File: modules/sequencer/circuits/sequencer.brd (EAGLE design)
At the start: 100 x 80 mm, 35 parts, among them IC2 LM324N

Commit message: sequencer design
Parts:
- added 1K, 1K1, 1K2, R23: 1k, adafruit:0207/12
- added 2N4400: (no value), transistor-neu-to92:TO92-EBC
- added DAISY_CHAIN, INPUTS: (no value), pinhead:1X06
- added MPS2907: (no value), transistor:TO92-CBE
- added R20: 10k, adafruit:0207/12
- added R21: 100k, adafruit:0207/12
- added RESET_BUTTON: (no value), pinhead:1X02
- added SPLIT_SELECT: (no value), pinhead:2X03
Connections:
- removed net VSS: CD4163.8
- new net COUNTER_POWER: CD4017.16, MPS2907.C
- new net HALF_STEP: 1K1.2, CD4163.11, R23.2
- new net N$2: CD4163.7, R20.2
- new net N$30: 1K.1, 2N4400.C, SPLIT_SELECT.3
- new net N$31: 2N4400.B, R23.1
- new net N$32: POWER.1, RESET_BUTTON.1
- new net N$36: 1K1.1, SPLIT_SELECT.5
- new net N$37: MPS2907.B, SPLIT_SELECT.2, SPLIT_SELECT.4, SPLIT_SELECT.6
- new net N$38: 1K2.1, SPLIT_SELECT.1
- net -12V: now also DAISY_CHAIN.4, INPUTS.4
- net 12V: now also DAISY_CHAIN.3, INPUTS.3
- net 3.3V: now also 2N4400.E, CD4017.15, CD4163.8, DAISY_CHAIN.6, INPUTS.6
- net 5V: now also 1K.2, 1K2.2, CD4163.16, DAISY_CHAIN.5, INPUTS.5, MPS2907.E, R20.1, R21.1, RESET_BUTTON.2; no longer CD4017.16, POWER.1
- net CLK_IN: now also CD4163.2, DAISY_CHAIN.1, INPUTS.1
- net N$10: now also R19.2; no longer R1.2
- net N$3: now also R1.2; no longer R19.2
- net N$4: now also R13.2; no longer R18.2
- net N$5: now also R14.2; no longer R17.2
- net N$6: now also R15.2; no longer R16.2
- net N$7: now also R16.2; no longer R15.2
- net N$8: now also R17.2; no longer R14.2
- net N$9: now also R18.2; no longer R13.2
- net RESET: now also CD4163.1, CD4163.9, R21.2; no longer CD4017.15
- net START_STOP: now also DAISY_CHAIN.2, INPUTS.2
- net VDD: no longer CD4163.16

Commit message: Sync
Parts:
- removed C3: 2.2uf, adafruit:E2,5-6E
- removed C4: 1uf, adafruit:E2,5-6E
- removed INPUTS: (no value), pinhead:1X06
- removed LM7905: (no value), linear:TO220H
- removed POWER: (no value), pinhead:1X04
- added 1: 4017N, 40xx:DIL16
- added D10, D11, D12, D13, D14, D15, D16, D9: 1N4004, adafruit:DO41-10
- added INPUTS1: (no value), pinhead:1X06
- added R40, R56: 10k, SparkFun-Resistors:AXIAL-0.3
- added R41, R42, R43, R44, R45, R46, R47, R48, R49, R50, R51, R52, R53, R54, R55: 1k, SparkFun-Resistors:AXIAL-0.3
- added WIDTH_SELECTION1: (no value), pinhead:2X07
- moved CD4163 66.1 mm to (83.8, 14.0)
- moved DAISY_CHAIN 6.35 mm to (-74.9, -213.4)
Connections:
- removed net -5V: C4.-, IC2.11, LM7905.3
- removed net START_STOP: CD4017.13, DAISY_CHAIN.2, INPUTS.2
- removed net VDD: C3.-, LM7905.2
- new net DIV_CLK: CD4017.14, D10.C, D11.C, D12.C, D9.C, DAISY_CHAIN.1, R40.P$1
- new net GATE_OUT: R47.P$2, R48.P$2, R56.P$1
- new net GND: 1.13, 1.8
- new net GNDA: R40.P$2, R56.P$2, WIDTH_SELECTION1.10, WIDTH_SELECTION1.12, WIDTH_SELECTION1.14, WIDTH_SELECTION1.2, WIDTH_SELECTION1.4, WIDTH_SELECTION1.6, WIDTH_SELECTION1.8
- new net N$56: 1.15, 1.9
- new net N$57: 1.3, D16.A, D9.A
- new net N$58: 1.2, D10.A, D13.A
- new net N$59: 1.4, D11.A, D14.A
- new net N$60: 1.7, D12.A, D15.A
- new net N$61: 1.6, R48.P$1
- new net N$62: R41.P$2, R47.P$1, R49.P$2, WIDTH_SELECTION1.13
- new net N$63: R41.P$1, R42.P$2, R50.P$2, WIDTH_SELECTION1.11
- new net N$64: 1.10, R51.P$1
- new net N$65: R43.P$1, R44.P$2, R52.P$2, WIDTH_SELECTION1.7
- new net N$66: R44.P$1, R45.P$2, R53.P$2, WIDTH_SELECTION1.5
- new net N$67: R45.P$1, R46.P$2, R54.P$2, WIDTH_SELECTION1.3
- new net N$68: R46.P$1, R55.P$2, WIDTH_SELECTION1.1
- new net N$69: 1.5, R49.P$1
- new net N$70: 1.1, R50.P$1
- new net N$71: R42.P$1, R43.P$2, R51.P$2, WIDTH_SELECTION1.9
- new net N$72: D15.C, R52.P$1
- new net N$73: D14.C, R53.P$1
- new net N$74: D13.C, R54.P$1
- new net N$75: D16.C, R55.P$1
- net -12V: now also IC2.11, INPUTS1.3; no longer INPUTS.4, POWER.3
- net 12V: now also IC2.4, INPUTS1.2; no longer INPUTS.3, POWER.2
- net 3.3V: now also INPUTS1.4; no longer C3.+, C4.+, INPUTS.6, LM7905.1, POWER.4
- net 5V: now also 1.16; no longer IC2.4, INPUTS.5
- net CLK_IN: now also 1.14, INPUTS1.5; no longer CD4017.14, DAISY_CHAIN.1, INPUTS.1
- net N$32: now also INPUTS1.1; no longer POWER.1

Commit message: divider
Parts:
- removed 1: 4017N, 40xx:DIL16
- removed D10, D11, D12, D13, D14, D15, D16, D9: 1N4004, adafruit:DO41-10
- removed R40, R56: 10k, SparkFun-Resistors:AXIAL-0.3
- removed R41, R42, R43, R44, R45, R46, R47, R48, R49, R50, R51, R52, R53, R54, R55: 1k, SparkFun-Resistors:AXIAL-0.3
- removed WIDTH_SELECTION1: (no value), pinhead:2X07
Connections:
- removed net DIV_CLK: CD4017.14, D10.C, D11.C, D12.C, D9.C, DAISY_CHAIN.1, R40.P$1
- removed net GATE_OUT: R47.P$2, R48.P$2, R56.P$1
- removed net GND: 1.13, 1.8
- removed net GNDA: R40.P$2, R56.P$2, WIDTH_SELECTION1.10, WIDTH_SELECTION1.12, WIDTH_SELECTION1.14, WIDTH_SELECTION1.2, WIDTH_SELECTION1.4, WIDTH_SELECTION1.6, WIDTH_SELECTION1.8
- removed net N$56: 1.15, 1.9
- removed net N$57: 1.3, D16.A, D9.A
- removed net N$58: 1.2, D10.A, D13.A
- removed net N$59: 1.4, D11.A, D14.A
- removed net N$60: 1.7, D12.A, D15.A
- removed net N$61: 1.6, R48.P$1
- removed net N$62: R41.P$2, R47.P$1, R49.P$2, WIDTH_SELECTION1.13
- removed net N$63: R41.P$1, R42.P$2, R50.P$2, WIDTH_SELECTION1.11
- removed net N$64: 1.10, R51.P$1
- removed net N$65: R43.P$1, R44.P$2, R52.P$2, WIDTH_SELECTION1.7
- removed net N$66: R44.P$1, R45.P$2, R53.P$2, WIDTH_SELECTION1.5
- removed net N$67: R45.P$1, R46.P$2, R54.P$2, WIDTH_SELECTION1.3
- removed net N$68: R46.P$1, R55.P$2, WIDTH_SELECTION1.1
- removed net N$69: 1.5, R49.P$1
- removed net N$70: 1.1, R50.P$1
- removed net N$71: R42.P$1, R43.P$2, R51.P$2, WIDTH_SELECTION1.9
- removed net N$72: D15.C, R52.P$1
- removed net N$73: D14.C, R53.P$1
- removed net N$74: D13.C, R54.P$1
- removed net N$75: D16.C, R55.P$1
- net 5V: no longer 1.16
- net CLK_IN: now also CD4017.14, DAISY_CHAIN.1; no longer 1.14

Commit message: Sequencer design complete
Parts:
- removed MPS2907: (no value), transistor:TO92-CBE
- added 1K3, 1K4: 1k, adafruit:0207/12
- added 2N1, 2N2: (no value), transistor-neu-to92:TO92-EBC
- added C2: 220uf, rcl:E2,5-6E
- added C3: 100nf, rcl:C025-024X044
- added D1: 1N4004, adafruit:DO41-10
- added GATE_POT, OUT, RESET_AFTER_2, RESET_AFTER_4: (no value), pinhead:1X02
- added R22, R24, R25: 10k, adafruit:0207/12
- moved INPUTS1 319.1 mm to (38.1, 7.62)
- moved RESET_BUTTON 267.8 mm to (50.8, 7.62)
- moved SPLIT_SELECT 259.7 mm to (43.2, 29.2)
- moved 1K2 255.6 mm to (40.6, 19.1), turned to 270 degrees
- moved 2N4400 245.5 mm to (62.2, 26.7), turned to 90 degrees
- moved 1K1 245.4 mm to (45.7, 19.1), turned to 270 degrees
- moved R21 244.3 mm to (72.4, 39.4), turned to 270 degrees
- moved R23 242.0 mm to (48.3, 19.1), turned to 270 degrees
- moved DAISY_CHAIN 241.1 mm to (21.6, 7.62)
- moved 1K 235.2 mm to (43.2, 19.1), turned to 270 degrees
- moved LED2 210.3 mm to (55.9, 66.0)
- moved LED3 210.3 mm to (55.9, 58.4)
- moved LED5 210.3 mm to (55.9, 43.2)
- moved LED6 210.3 mm to (55.9, 35.6)
- moved LED7 210.3 mm to (55.9, 27.9)
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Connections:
- removed net 3.3V: 2N4400.E, CD4017.15, CD4017.8, CD4163.8, DAISY_CHAIN.6, IC2.3, IC2.5, INPUTS1.4, LED1.K, LED2.K, LED3.K, LED4.K, LED5.K, LED6.K, LED7.K, LED8.K, POTS.17
- new net GATE: OUT.2, R24.1
- new net GND: 2N1.E, 2N2.E, 2N4400.E, CD4017.13, CD4017.8, CD4163.8, DAISY_CHAIN.6, IC2.3, IC2.5, INPUTS1.4, LED1.K, LED2.K, LED3.K, LED4.K, LED5.K, LED6.K, LED7.K, LED8.K, POTS.17, R20.1, R22.2
- new net N$35: 2N2.B, D1.C, R24.2
- new net N$39: 2N2.C, C2.+, R25.1
- new net N$40: 1K3.1, 2N1.C
- new net N$41: 1K4.1, GATE_POT.2
- new net N$42: 2N1.B, C2.-, GATE_POT.1
- net 5V: now also 1K3.2, 1K4.2, R25.2; no longer MPS2907.E, R20.1
- net CLK_IN: now also C3.1
- net COUNTER_POWER: now also IC2.8, IC2.9; no longer MPS2907.C
- net CV_OUT: now also OUT.1
- net N$1: now also CD4017.15, CD4017.9, R22.1, RESET_AFTER_2.1, RESET_AFTER_4.1; no longer CD4017.12, CD4163.3
- net N$2: now also C3.2, D1.A; no longer CD4163.7
- net N$37: now also IC2.10; no longer MPS2907.B
- net N$5: now also RESET_AFTER_2.2
- net N$8: now also RESET_AFTER_4.2
- net RESET: now also CD4163.7
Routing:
- net GND: track 0.00 -> 253.9 mm
- net CLK_IN: track 0.00 -> 200.7 mm
- net 5V: track 0.00 -> 109.7 mm
- net COUNTER_POWER: track 0.00 -> 72.1 mm
- net N$10: track 0.00 -> 71.6 mm
- net HALF_STEP: track 0.00 -> 69.2 mm
- net N$5: track 0.00 -> 67.0 mm
- net N$35: track 0.00 -> 66.9 mm
- net CV_OUT: track 0.00 -> 56.9 mm
- net N$7: track 0.00 -> 53.7 mm, vias 0 -> 1
- net N$4: track 0.00 -> 50.1 mm
- net N$3: track 0.00 -> 49.1 mm
- net RESET: track 0.00 -> 48.8 mm
- net N$9: track 0.00 -> 46.6 mm
- net N$6: track 0.00 -> 44.8 mm
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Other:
- board size 100 x 80 mm -> 68.2 x 80 mm

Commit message: Seq board
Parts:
- removed 1K, 1K2: 1k, adafruit:0207/12
- removed 2N1, 2N4400: (no value), transistor-neu-to92:TO92-EBC
- removed C3: 100nf, rcl:C025-024X044
- removed CD4163: 4163N, 40xx:DIL16
- removed DAISY_CHAIN: (no value), pinhead:1X06
- removed R24, R25: 10k, adafruit:0207/12
- removed SPLIT_SELECT: (no value), pinhead:2X03
- added C1: 0.01uf, rcl:C025-024X044
- added C4: 0.1uf, rcl:C025-024X044
- added IC1: LM555N, adafruit:DIL08-ROUND
- added LED9: (no value), adafruit:LED5MM
- 1K1: value 1k -> 100k
- 1K4: value 1k -> 10k
- D1: device adafruit:DO41-10 -> diode:DO41-10
- R21: value 100k -> 100
- R23: value 1k -> 330
- moved R21 191.6 mm to (15.2, -143.5), turned to 0 degrees
- moved 1K1 182.9 mm to (15.2, -161.3), turned to 0 degrees
- moved D1 179.1 mm to (14.0, -174.0)
- moved R23 178.3 mm to (15.2, -156.2), turned to 0 degrees
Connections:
- removed net COUNTER_POWER: CD4017.16, IC2.8, IC2.9
- removed net HALF_STEP: 1K1.2, CD4163.11, R23.2
- removed net N$37: IC2.10, SPLIT_SELECT.2, SPLIT_SELECT.4, SPLIT_SELECT.6
- removed net N$38: 1K2.1, SPLIT_SELECT.1
- removed net N$39: 2N2.C, C2.+, R25.1
- removed net N$40: 1K3.1, 2N1.C
- removed net N$41: 1K4.1, GATE_POT.2
- removed net N$42: 2N1.B, C2.-, GATE_POT.1
- removed net RESET: CD4163.1, CD4163.10, CD4163.7, CD4163.9, R21.2
- new net N$33: C4.1, D1.A, IC1.2, R20.1
- new net N$34: C1.1, IC1.5
- net -12V: no longer DAISY_CHAIN.4
- net 12V: no longer DAISY_CHAIN.3
- net 5V: now also C2.+, CD4017.16, D1.C, IC1.4, IC1.8, INPUTS1.1, R20.2, RESET_BUTTON.1; no longer 1K.2, 1K2.2, 1K3.2, CD4163.16, DAISY_CHAIN.5, R21.1, R25.2, RESET_BUTTON.2
- net CLK_IN: now also 2N2.B; no longer C3.1, CD4163.2, DAISY_CHAIN.1
- net GATE: now also 1K1.2; no longer R24.1
- net GND: now also C1.2, GATE_POT.1, IC1.1, R23.1; no longer 2N1.E, 2N4400.E, CD4163.8, DAISY_CHAIN.6, R20.1
- net N$1: now also RESET_BUTTON.2
- net N$10: no longer R19.2
- net N$2: now also 1K3.1, C4.2; no longer C3.2, D1.A, R20.2
- net N$3: no longer R1.2
- net N$30: now also LED9.K, R23.2; no longer 1K.1, 2N4400.C, SPLIT_SELECT.3
- net N$31: now also GATE_POT.2, R21.1; no longer 2N4400.B, R23.1
- net N$32: now also 1K3.2, 1K4.1, 2N2.C; no longer INPUTS1.1, RESET_BUTTON.1
- net N$35: now also C2.-, IC1.6, IC1.7, R21.2; no longer 2N2.B, D1.C, R24.2
- net N$36: now also IC1.3, LED9.A; no longer SPLIT_SELECT.5
- net N$4: no longer R13.2
- net N$5: no longer R14.2
- net N$6: no longer R15.2
- net N$7: no longer R16.2
- net N$8: no longer R17.2
- net N$9: no longer R18.2
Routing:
- net COUNTER_POWER: track 72.1 -> 0.00 mm
- net HALF_STEP: track 69.2 -> 0.00 mm
- net N$35: track 66.9 -> 0.00 mm
- net RESET: track 48.8 -> 0.00 mm
- net N$42: track 44.8 -> 0.00 mm
- net 5V: track 109.7 -> 66.7 mm
- net N$37: track 36.1 -> 0.00 mm
- net N$40: track 34.6 -> 0.00 mm
- net GND: track 253.9 -> 225.5 mm
- net N$39: track 27.5 -> 0.00 mm
- net N$41: track 25.9 -> 0.00 mm
- net N$30: track 23.4 -> 0.00 mm
- net N$32: track 19.8 -> 0.00 mm
- net CLK_IN: track 200.7 -> 183.1 mm
- net N$6: track 44.8 -> 28.2 mm
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
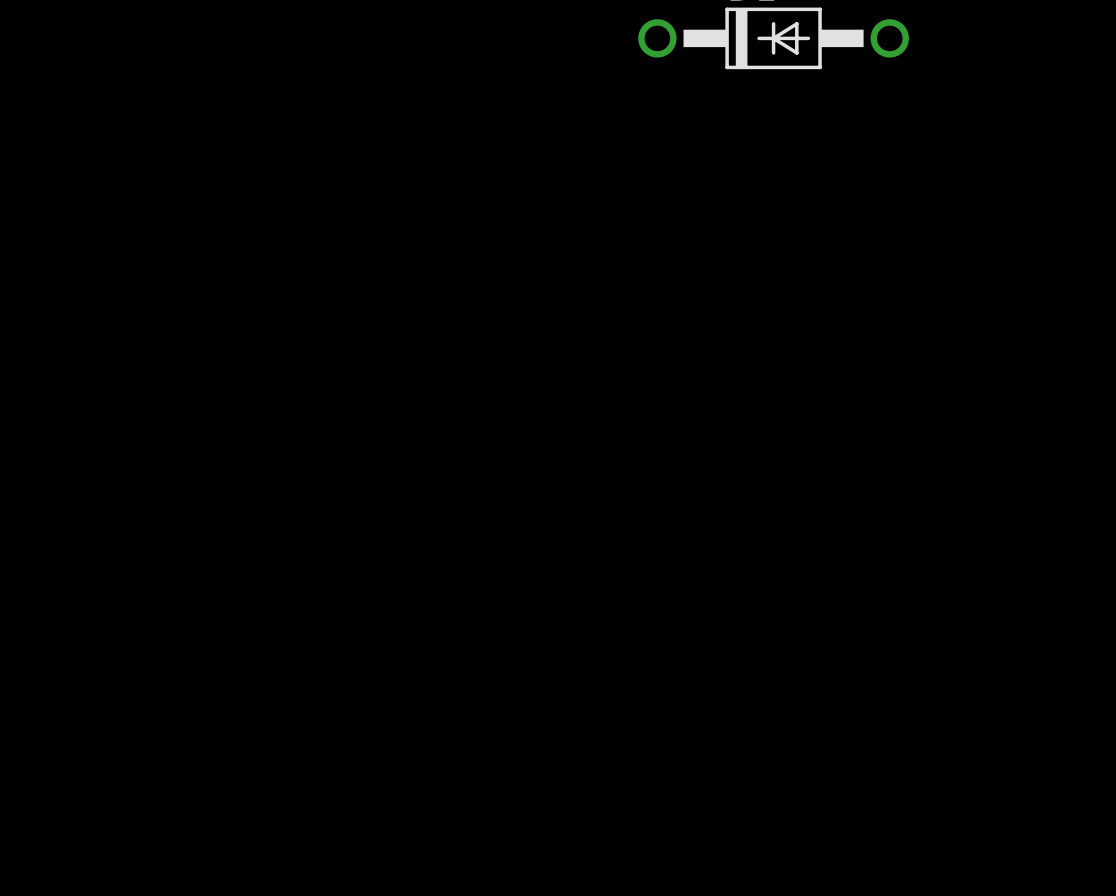
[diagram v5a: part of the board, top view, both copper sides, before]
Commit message: Adding counter to seq
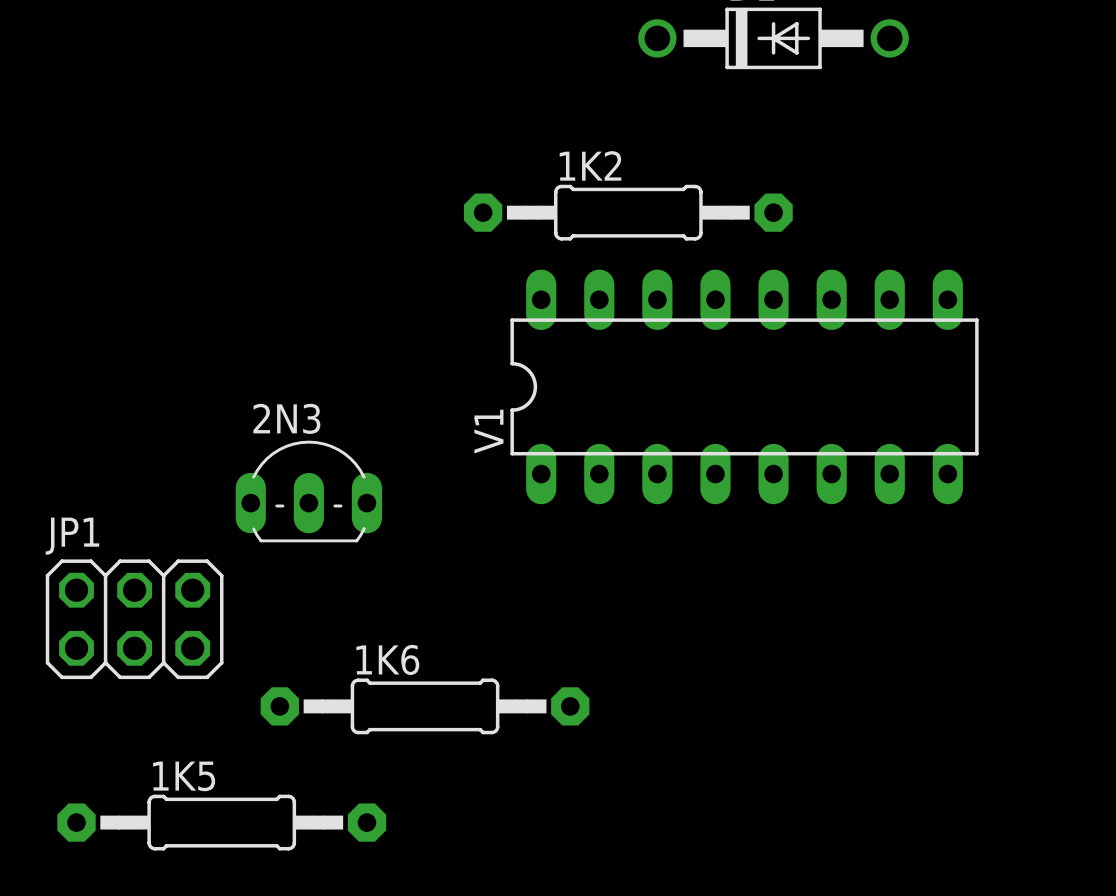
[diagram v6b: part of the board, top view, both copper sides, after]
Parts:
- added 1K2, 1K6: 1k, adafruit:0207/12
- added 1K5: 10k, adafruit:0207/12
- added 2N3: (no value), transistor-neu-to92:TO92-EBC
- added JP1: (no value), pinhead:2X03
- added V1: 74161N, 74ttl-din:DIL16
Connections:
- new net +UB: V1.16
- new net -UB: V1.8
- new net COUNTER_POWER: IC2.8, IC2.9
- new net N$37: 1K5.2, 2N3.B
- new net N$38: 1K5.1, JP1.4, V1.11
- new net N$39: 1K2.2, 1K6.2, 2N3.C
- new net N$40: 1K2.1, JP1.6
- new net N$42: IC2.10, JP1.1, JP1.3, JP1.5
- new net Q1: V1.14
- new net Q2: V1.13
- new net Q3: V1.12
- net 5V: now also 1K6.1, JP1.2
- net CLK_IN: now also V1.2
- net GND: now also 2N3.E
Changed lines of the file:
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@@
 <?xml version="1.0" encoding="utf-8"?>
 <!DOCTYPE eagle SYSTEM "eagle.dtd">
-<eagle version="9.6.2">
+<eagle version="9.5.2">
 <drawing>
 <settings>
@@
 <attribute name="VALUE" x="11.938" y="-176.784" size="1.27" layer="27" ratio="10"/>
 </element>
+<element name="1K2" library="adafruit" library_urn="urn:adsk.eagle:library:420" package="0207/12" package3d_urn="urn:adsk.eagle:package:6240598/1" value="1k" x="7.62" y="-181.61" smashed="yes">
+<attribute name="NAME" x="4.445" y="-180.213" size="1.27" layer="25" ratio="10"/>
+<attribute name="VALUE" x="5.334" y="-182.2958" size="1.27" layer="27" ratio="10"/>
+</element>
+<element name="V1" library="74ttl-din" library_urn="urn:adsk.eagle:library:84" package="DIL16" package3d_urn="urn:adsk.eagle:package:922/2" value="74161N" x="12.7" y="-189.23" smashed="yes">
+<attribute name="NAME" x="2.159" y="-192.151" size="1.27" layer="25" ratio="10" rot="R90"/>
+<attribute name="POPULARITY" value="0" x="12.7" y="-189.23" size="1.778" layer="27" display="off"/>
+<attribute name="VALUE" x="5.207" y="-189.865" size="1.27" layer="27" ratio="10"/>
+</element>
+<element name="2N3" library="transistor-neu-to92" library_urn="urn:adsk.eagle:library:397" package="TO92-EBC" package3d_urn="urn:adsk.eagle:package:28763/2" value="" x="-6.35" y="-193.04" smashed="yes">
+<attribute name="NAME" x="-8.89" y="-191.262" size="1.27" layer="25" ratio="10"/>
+<attribute name="POPULARITY" value="0" x="-6.35" y="-193.04" size="1.778" layer="27" display="off"/>
+<attribute name="VALUE" x="-8.89" y="-197.612" size="1.27" layer="27" ratio="10"/>
+</element>
+<element name="1K6" library="adafruit" library_urn="urn:adsk.eagle:library:420" package="0207/12" package3d_urn="urn:adsk.eagle:package:6240598/1" value="1k" x="-1.27" y="-203.2" smashed="yes">
+<attribute name="NAME" x="-4.445" y="-201.803" size="1.27" layer="25" ratio="10"/>
+<attribute name="VALUE" x="-3.556" y="-203.8858" size="1.27" layer="27" ratio="10"/>
+</element>
+<element name="JP1" library="pinhead" library_urn="urn:adsk.eagle:library:325" package="2X03" package3d_urn="urn:adsk.eagle:package:22462/2" value="" x="-13.97" y="-199.39" smashed="yes">
+<attribute name="NAME" x="-17.78" y="-196.215" size="1.27" layer="25" ratio="10"/>
+<attribute name="POPULARITY" value="62" x="-13.97" y="-199.39" size="1.778" layer="27" display="off"/>
+<attribute name="VALUE" x="-17.78" y="-203.835" size="1.27" layer="27"/>
+</element>
+<element name="1K5" library="adafruit" library_urn="urn:adsk.eagle:library:420" package="0207/12" package3d_urn="urn:adsk.eagle:package:6240598/1" value="10k" x="-10.16" y="-208.28" smashed="yes">
+<attribute name="NAME" x="-13.335" y="-206.883" size="1.27" layer="25" ratio="10"/>
+<attribute name="VALUE" x="-12.446" y="-208.9658" size="1.27" layer="27" ratio="10"/>
+</element>
 </elements>
 <signals>
@@
 <wire x1="60.96" y1="12.7" x2="60.96" y2="10.16" width="0.1524" layer="1"/>
 <contactref element="R23" pad="1"/>
+<contactref element="2N3" pad="E"/>
+<wire x1="8.89" y1="-156.21" x2="-8.89" y2="-194.31" width="0" layer="19" extent="1-1"/>
 <wire x1="11.43" y1="-135.89" x2="8.89" y2="-156.21" width="0" layer="19" extent="1-1"/>
 <wire x1="11.43" y1="-130.81" x2="11.43" y2="-135.89" width="0" layer="19" extent="1-1"/>
@@
 <contactref element="C2" pad="+"/>
 <contactref element="D1" pad="C"/>
+<contactref element="1K6" pad="1"/>
+<contactref element="JP1" pad="2"/>
+<wire x1="-7.62" y1="-203.2" x2="-16.51" y2="-198.12" width="0" layer="19" extent="1-1"/>
+<wire x1="8.89" y1="-173.99" x2="-7.62" y2="-203.2" width="0" layer="19" extent="1-1"/>
 <wire x1="19.05" y1="-130.81" x2="8.89" y2="-173.99" width="0" layer="19" extent="1-1"/>
 <wire x1="11.43" y1="-123.19" x2="19.05" y2="-130.81" width="0" layer="19" extent="1-1"/>
@@
 <wire x1="38.1" y1="3.81" x2="19.05" y2="3.81" width="0.1524" layer="1"/>
 <contactref element="2N2" pad="B"/>
-<wire x1="54.61" y1="5.08" x2="69.85" y2="5.08" width="0" layer="19" extent="1-1"/>
+<contactref element="V1" pad="2"/>
+<wire x1="19.05" y1="3.81" x2="6.35" y2="-193.04" width="0" layer="19" extent="1-1"/>
 <wire x1="10.16" y1="7.62" x2="19.05" y2="3.81" width="0" layer="19" extent="1-1"/>
+<wire x1="69.85" y1="5.08" x2="54.61" y2="5.08" width="0" layer="19" extent="1-1"/>
 </signal>
 <signal name="N$3">
@@
 <wire x1="66.04" y1="7.62" x2="8.89" y2="-143.51" width="0" layer="19" extent="1-1"/>
 </signal>
+<signal name="+UB">
+<contactref element="V1" pad="16"/>
+</signal>
+<signal name="-UB">
+<contactref element="V1" pad="8"/>
+</signal>
+<signal name="N$38">
+<contactref element="V1" pad="11"/>
+<contactref element="JP1" pad="4"/>
+<contactref element="1K5" pad="1"/>
+<wire x1="-13.97" y1="-198.12" x2="-16.51" y2="-208.28" width="0" layer="19" extent="1-1"/>
+<wire x1="16.51" y1="-185.42" x2="-13.97" y2="-198.12" width="0" layer="19" extent="1-1"/>
+</signal>
+<signal name="N$39">
+<contactref element="1K6" pad="2"/>
+<contactref element="2N3" pad="C"/>
+<contactref element="1K2" pad="2"/>
+<wire x1="-3.81" y1="-194.31" x2="5.08" y2="-203.2" width="0" layer="19" extent="1-1"/>
+<wire x1="13.97" y1="-181.61" x2="-3.81" y2="-194.31" width="0" layer="19" extent="1-1"/>
+</signal>
+<signal name="N$40">
+<contactref element="1K2" pad="1"/>
+<contactref element="JP1" pad="6"/>
+<wire x1="1.27" y1="-181.61" x2="-11.43" y2="-198.12" width="0" layer="19" extent="1-1"/>
+</signal>
+<signal name="N$42">
+<contactref element="JP1" pad="5"/>
+<contactref element="JP1" pad="3"/>
+<contactref element="JP1" pad="1"/>
+<contactref element="IC2" pad="10"/>
+<wire x1="-13.97" y1="-200.66" x2="-16.51" y2="-200.66" width="0" layer="19" extent="1-1"/>
+<wire x1="-11.43" y1="-200.66" x2="-13.97" y2="-200.66" width="0" layer="19" extent="1-1"/>
+<wire x1="22.86" y1="13.97" x2="-11.43" y2="-200.66" width="0" layer="19" extent="1-1"/>
+</signal>
+<signal name="COUNTER_POWER">
+<contactref element="IC2" pad="8"/>
+<contactref element="IC2" pad="9"/>
+<wire x1="17.78" y1="13.97" x2="20.32" y2="13.97" width="0" layer="19" extent="1-1"/>
+</signal>
+<signal name="N$37">
+<contactref element="2N3" pad="B"/>
+<contactref element="1K5" pad="2"/>
+<wire x1="-6.35" y1="-194.31" x2="-3.81" y2="-208.28" width="0" layer="19" extent="1-1"/>
+</signal>
+<signal name="Q1">
+<contactref element="V1" pad="14"/>
+</signal>
+<signal name="Q2">
+<contactref element="V1" pad="13"/>
+</signal>
+<signal name="Q3">
+<contactref element="V1" pad="12"/>
+</signal>
 </signals>
